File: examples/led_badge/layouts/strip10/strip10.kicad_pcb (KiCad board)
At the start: 2 copper layers, 20 parts

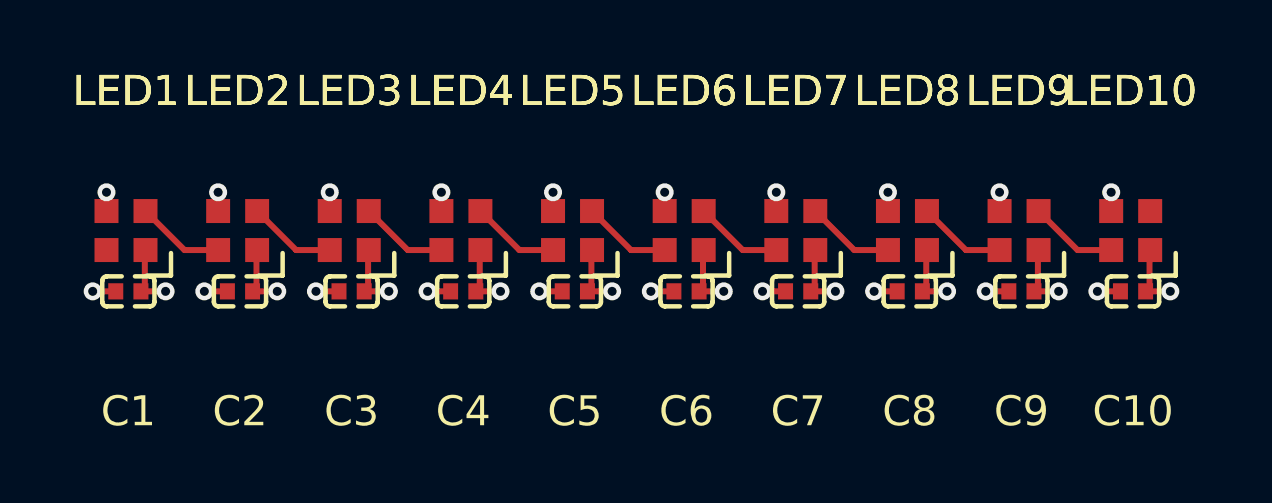
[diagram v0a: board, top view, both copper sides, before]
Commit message: Restore Atopile Local 0.2 on pinned 0.15.9 sources
Import the publicly distributed atopile 0.15.9 PyPI source release as the
compiler/UI baseline, retaining upstream main as its historical parent.
PyPI source SHA256: 681cc1e123646dd133de31b631aedaf4eaac88682613b4f82d1da4b3ef8b4e8e.

Revive the local VS Code extension with a separate identity and launcher,
isolated state, bundled visualization assets, and provider settings. Bridge
the existing Atopile tool harness to a natively signed-in Codex app-server
for ChatGPT-plan use, retaining direct API providers as explicit options.
Include local part import, layout tools, packaging/runtime setup and tests.

Preserve upstream licensing, restored GitHub metadata and source notices.
Exclude local environments, generated webview bundles and personal QA paths.
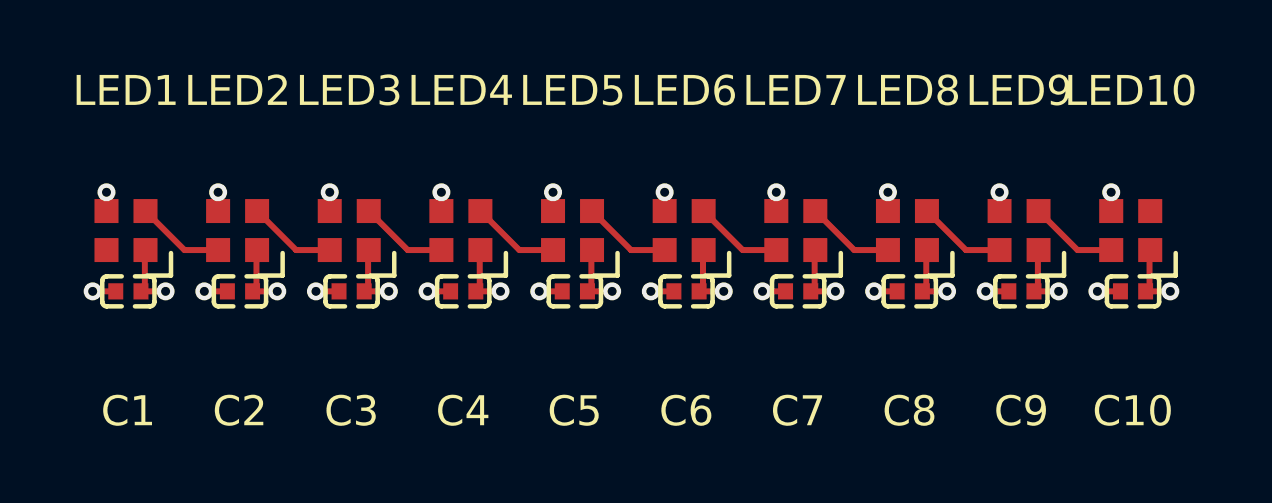
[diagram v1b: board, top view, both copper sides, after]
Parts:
- C1, C10, C2, C3, C4, C5, C6, C7, C8, C9: value 100nF -> 100nF ±10%
